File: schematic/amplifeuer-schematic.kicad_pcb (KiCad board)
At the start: 2 copper layers, 16 parts, among them J1 Input, J3 Output1, J4 Output2, J5 Power, U1 TDA1521A

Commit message: Move amplifier schematic 1 layer down
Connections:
- net +12V renamed /amplifier/+Vp
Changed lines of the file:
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@@
   (net 9 "Net-(C5-Pad2)")
   (net 10 GND)
-  (net 11 +12V)
-  (net 12 "Net-(C9-Pad1)")
-  (net 13 "Net-(C6-Pad2)")
+  (net 11 "Net-(C9-Pad1)")
+  (net 12 "Net-(C6-Pad2)")
+  (net 13 /amplifier/+Vp)
   (net_class Default "This is the default net class."
     (clearance 0.2)
@@
     (uvia_dia 0.3)
     (uvia_drill 0.1)
-    (add_net +12V)
+    (add_net /amplifier/+Vp)
     (add_net GND)
     (add_net "Net-(C1-Pad1)")
@@
       (net 10 GND))
     (pad 1 thru_hole rect (at 0 0) (size 1.7 1.7) (drill 1) (layers *.Cu *.Mask)
-      (net 13 "Net-(C6-Pad2)"))
+      (net 12 "Net-(C6-Pad2)"))
     (model ${KISYS3DMOD}/Connector_PinHeader_2.54mm.3dshapes/PinHeader_1x02_P2.54mm_Vertical.wrl
       (at (xyz 0 0 0))
@@
       (net 10 GND))
     (pad 2 thru_hole oval (at 0 2.54) (size 1.7 1.7) (drill 1) (layers *.Cu *.Mask)
-      (net 11 +12V))
+      (net 13 /amplifier/+Vp))
     (model ${KISYS3DMOD}/Connector_PinHeader_2.54mm.3dshapes/PinHeader_1x02_P2.54mm_Vertical.wrl
       (at (xyz 0 0 0))
@@
       (net 1 "Net-(C1-Pad2)"))
     (pad 2 thru_hole oval (at 0 2.54 90) (size 1.7 1.7) (drill 1) (layers *.Cu *.Mask)
-      (net 12 "Net-(C9-Pad1)"))
+      (net 11 "Net-(C9-Pad1)"))
     (pad 3 thru_hole oval (at 0 5.08 90) (size 1.7 1.7) (drill 1) (layers *.Cu *.Mask)
-      (net 12 "Net-(C9-Pad1)"))
+      (net 11 "Net-(C9-Pad1)"))
     (pad 4 thru_hole oval (at 0 7.62 90) (size 1.7 1.7) (drill 1) (layers *.Cu *.Mask)
       (net 5 "Net-(C3-Pad1)"))
@@
       (net 9 "Net-(C5-Pad2)"))
     (pad 7 thru_hole oval (at 0 15.24 90) (size 1.7 1.7) (drill 1) (layers *.Cu *.Mask)
-      (net 11 +12V))
+      (net 13 /amplifier/+Vp))
     (pad 8 thru_hole oval (at 0 17.78 90) (size 1.7 1.7) (drill 1) (layers *.Cu *.Mask)
-      (net 12 "Net-(C9-Pad1)"))
+      (net 11 "Net-(C9-Pad1)"))
     (pad 9 thru_hole oval (at 0 20.32 90) (size 1.7 1.7) (drill 1) (layers *.Cu *.Mask)
       (net 4 "Net-(C2-Pad2)"))
@@
       (net 9 "Net-(C5-Pad2)"))
     (pad 2 thru_hole circle (at 5 0 270) (size 2 2) (drill 1) (layers *.Cu *.Mask)
-      (net 13 "Net-(C6-Pad2)"))
+      (net 12 "Net-(C6-Pad2)"))
     (model ${KISYS3DMOD}/Capacitor_THT.3dshapes/CP_Radial_D10.0mm_P5.00mm.wrl
       (at (xyz 0 0 0))
@@
     )
     (pad 1 thru_hole rect (at 0 0 270) (size 2 2) (drill 1) (layers *.Cu *.Mask)
-      (net 11 +12V))
+      (net 13 /amplifier/+Vp))
     (pad 2 thru_hole circle (at 5 0 270) (size 2 2) (drill 1) (layers *.Cu *.Mask)
       (net 10 GND))
@@
     )
     (pad 1 thru_hole circle (at 0 0 180) (size 2 2) (drill 1) (layers *.Cu *.Mask)
-      (net 11 +12V))
+      (net 13 /amplifier/+Vp))
     (pad 2 thru_hole circle (at 5 0 180) (size 2 2) (drill 1) (layers *.Cu *.Mask)
       (net 10 GND))
@@
     )
     (pad 1 thru_hole rect (at 0 0) (size 1.6 1.6) (drill 0.8) (layers *.Cu *.Mask)
-      (net 12 "Net-(C9-Pad1)"))
+      (net 11 "Net-(C9-Pad1)"))
     (pad 2 thru_hole circle (at 2.5 0) (size 1.6 1.6) (drill 0.8) (layers *.Cu *.Mask)
       (net 10 GND))
@@
   (segment (start 184.15 94) (end 187.865001 90.284999) (width 0.25) (layer B.Cu) (net 10))
   (segment (start 184.15 95.25) (end 184.15 94) (width 0.25) (layer B.Cu) (net 10))
-  (segment (start 171.45 74.93) (end 171.45 77.47) (width 0.25) (layer F.Cu) (net 11))
-  (segment (start 181.61 77.47) (end 186.69 82.55) (width 0.25) (layer B.Cu) (net 11))
-  (segment (start 171.45 77.47) (end 181.61 77.47) (width 0.25) (layer B.Cu) (net 11))
-  (segment (start 184.15 85.09) (end 186.69 82.55) (width 0.25) (layer F.Cu) (net 11))
-  (segment (start 184.15 90.25) (end 184.15 85.09) (width 0.25) (layer F.Cu) (net 11))
-  (segment (start 161.29 74.93) (end 158.75 74.93) (width 0.25) (layer F.Cu) (net 12))
-  (segment (start 162.139999 74.080001) (end 161.29 74.93) (width 0.25) (layer B.Cu) (net 12))
-  (segment (start 163.83 72.39) (end 162.139999 74.080001) (width 0.25) (layer B.Cu) (net 12))
-  (segment (start 171.45 72.39) (end 163.83 72.39) (width 0.25) (layer B.Cu) (net 12))
-  (segment (start 173.99 74.93) (end 171.45 72.39) (width 0.25) (layer B.Cu) (net 12))
-  (segment (start 161.29 71.12) (end 161.29 74.93) (width 0.25) (layer F.Cu) (net 12))
-  (segment (start 161.29 71.12) (end 161.29 68.58) (width 0.25) (layer F.Cu) (net 12))
-  (segment (start 176.53 85.09) (end 176.53 92.71) (width 0.25) (layer F.Cu) (net 13))
+  (segment (start 171.45 74.93) (end 171.45 77.47) (width 0.25) (layer F.Cu) (net 13))
+  (segment (start 181.61 77.47) (end 186.69 82.55) (width 0.25) (layer B.Cu) (net 13))
+  (segment (start 171.45 77.47) (end 181.61 77.47) (width 0.25) (layer B.Cu) (net 13))
+  (segment (start 184.15 85.09) (end 186.69 82.55) (width 0.25) (layer F.Cu) (net 13))
+  (segment (start 184.15 90.25) (end 184.15 85.09) (width 0.25) (layer F.Cu) (net 13))
+  (segment (start 161.29 74.93) (end 158.75 74.93) (width 0.25) (layer F.Cu) (net 11))
+  (segment (start 162.139999 74.080001) (end 161.29 74.93) (width 0.25) (layer B.Cu) (net 11))
+  (segment (start 163.83 72.39) (end 162.139999 74.080001) (width 0.25) (layer B.Cu) (net 11))
+  (segment (start 171.45 72.39) (end 163.83 72.39) (width 0.25) (layer B.Cu) (net 11))
+  (segment (start 173.99 74.93) (end 171.45 72.39) (width 0.25) (layer B.Cu) (net 11))
+  (segment (start 161.29 71.12) (end 161.29 74.93) (width 0.25) (layer F.Cu) (net 11))
+  (segment (start 161.29 71.12) (end 161.29 68.58) (width 0.25) (layer F.Cu) (net 11))
+  (segment (start 176.53 85.09) (end 176.53 92.71) (width 0.25) (layer F.Cu) (net 12))
 )

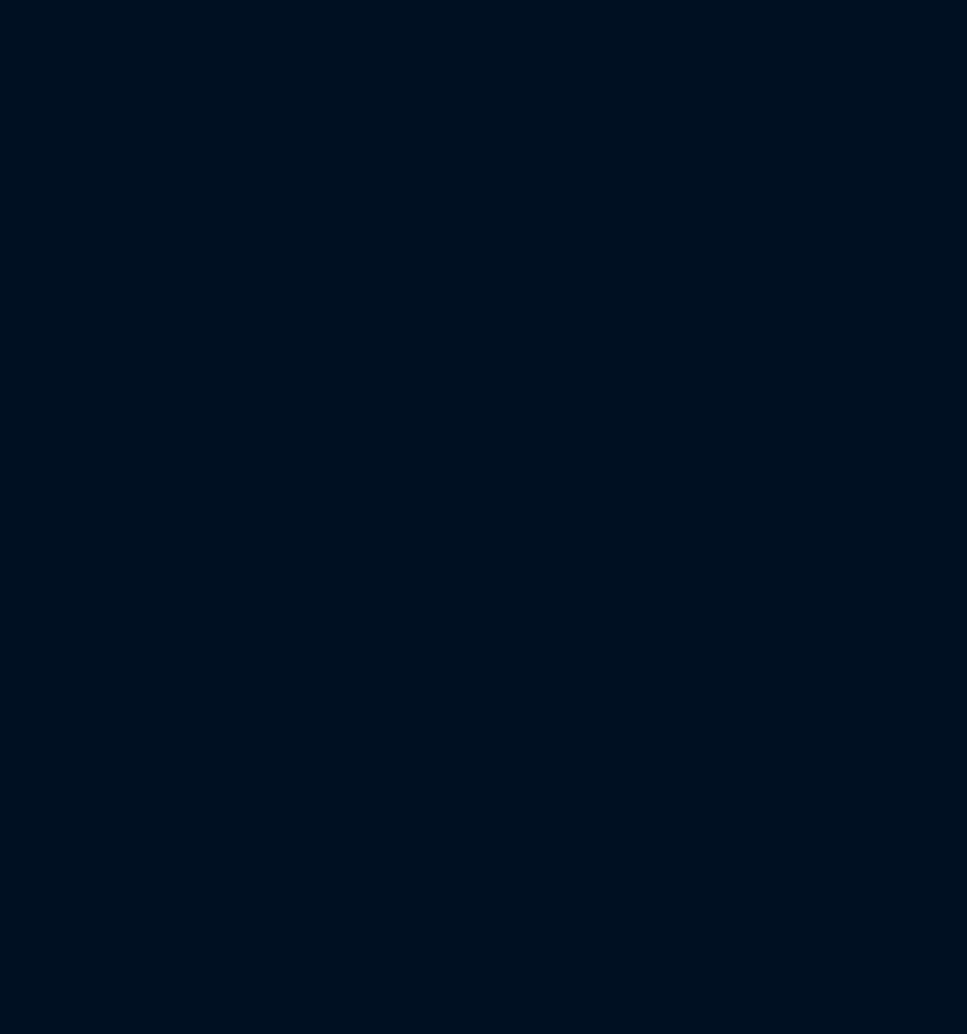
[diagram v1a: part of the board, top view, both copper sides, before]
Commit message: Add rudimentary PSU schematic and layout
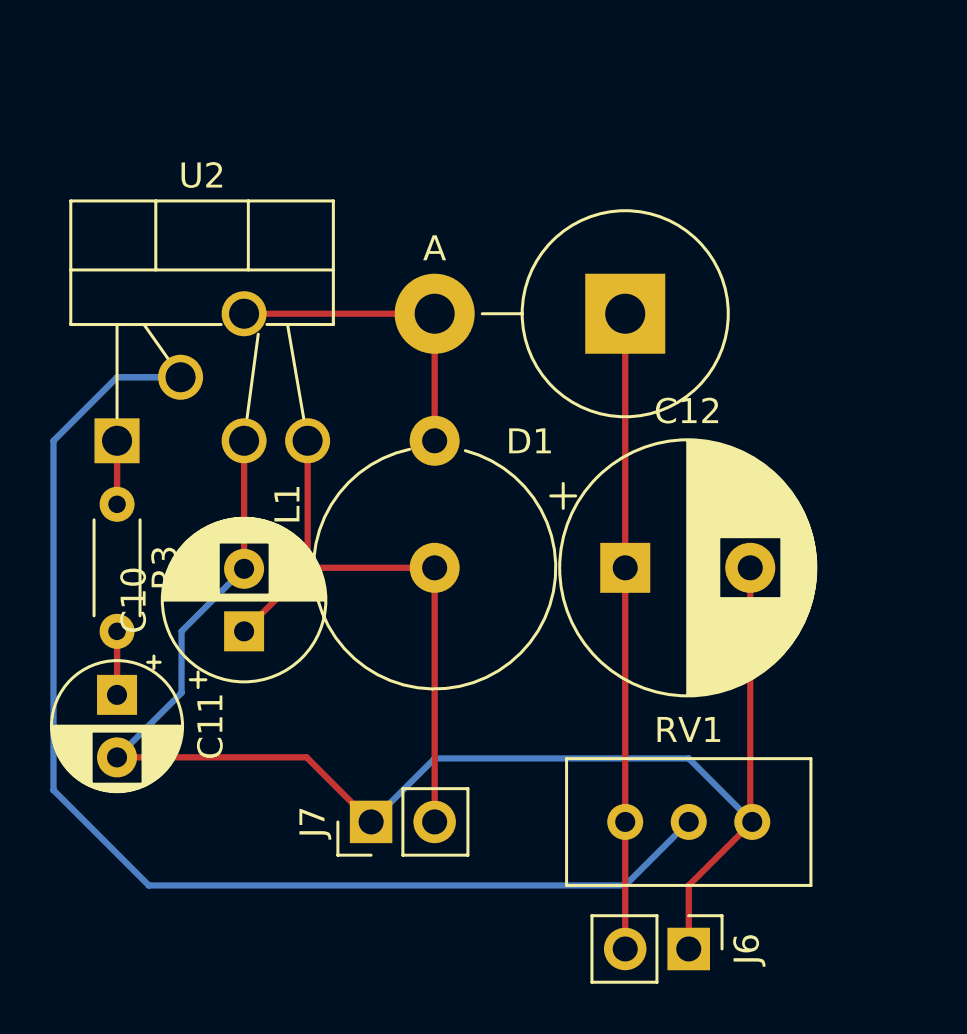
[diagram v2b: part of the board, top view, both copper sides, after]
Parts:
- added C10: 100μF, Capacitor_THT:CP_Radial_D6.3mm_P2.50mm, F.Cu at (105.4, 87.6)
- added C11: 1μF, Capacitor_THT:CP_Radial_D5.0mm_P2.50mm, F.Cu at (100.3, 90.2)
- added C12: 1000μF, Capacitor_THT:CP_Radial_D10.0mm_P5.00mm, F.Cu at (120.7, 85.1)
- added D1: D_Schottky, Diode_THT:D_5KPW_P7.62mm_Vertical_AnodeUp, F.Cu at (120.7, 74.9)
- added J6: Power out, Connector_PinHeader_2.54mm:PinHeader_1x02_P2.54mm_Vertical, F.Cu at (123.2, 100.3)
- added J7: Power in, Connector_PinHeader_2.54mm:PinHeader_1x02_P2.54mm_Vertical, F.Cu at (110.5, 95.2)
- added L1: L_Core_Ferrite, Inductor_THT:L_Axial_L16.0mm_D9.5mm_P5.08mm_Vertical_Vishay_IM-10-37, F.Cu at (113.0, 85.1)
- added R3: 1000R, Resistor_THT:R_Axial_DIN0204_L3.6mm_D1.6mm_P5.08mm_Horizontal, F.Cu at (100.3, 82.5)
- added RV1: R_POT_TRIM, Potentiometer_THT:Potentiometer_Bourns_3296W_Vertical, F.Cu at (125.7, 95.2)
- added U2: LT1071, Package_TO_SOT_THT:TO-220-5_PitchAligned, F.Cu at (100.3, 80.0)
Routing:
- net GND: track 94.5 -> 253.9 mm
- net /amplifier/+Vp: track 28.6 -> 167.4 mm
- net Net-(RV1-Pad2): track 0.00 -> 48.1 mm
- net +12V: track 0.00 -> 23.9 mm
- net Net-(D1-Pad2): track 0.00 -> 12.7 mm
- net Net-(C11-Pad1): track 0.00 -> 2.54 mm
- net Net-(R3-Pad1): track 0.00 -> 2.54 mm
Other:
- copper layers 2 -> 4

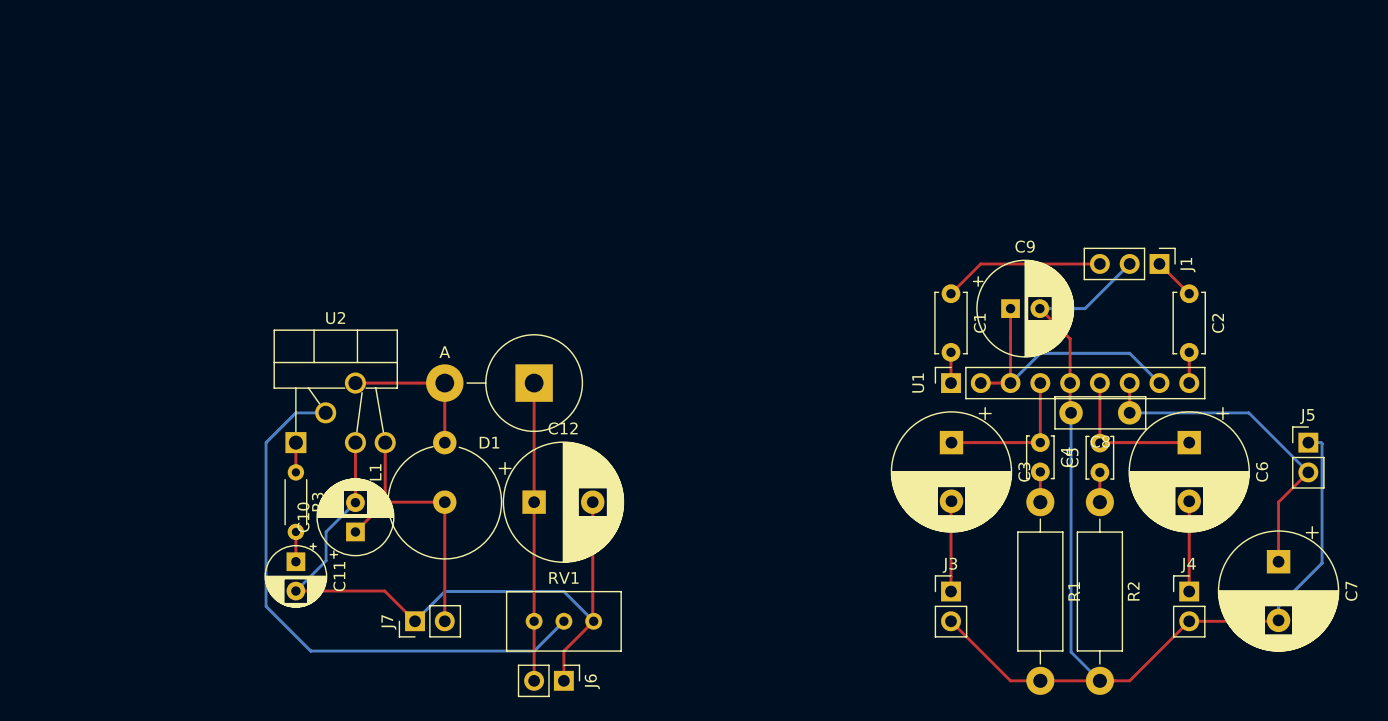
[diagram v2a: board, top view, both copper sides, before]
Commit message: Update all models on PCB to use WRL models
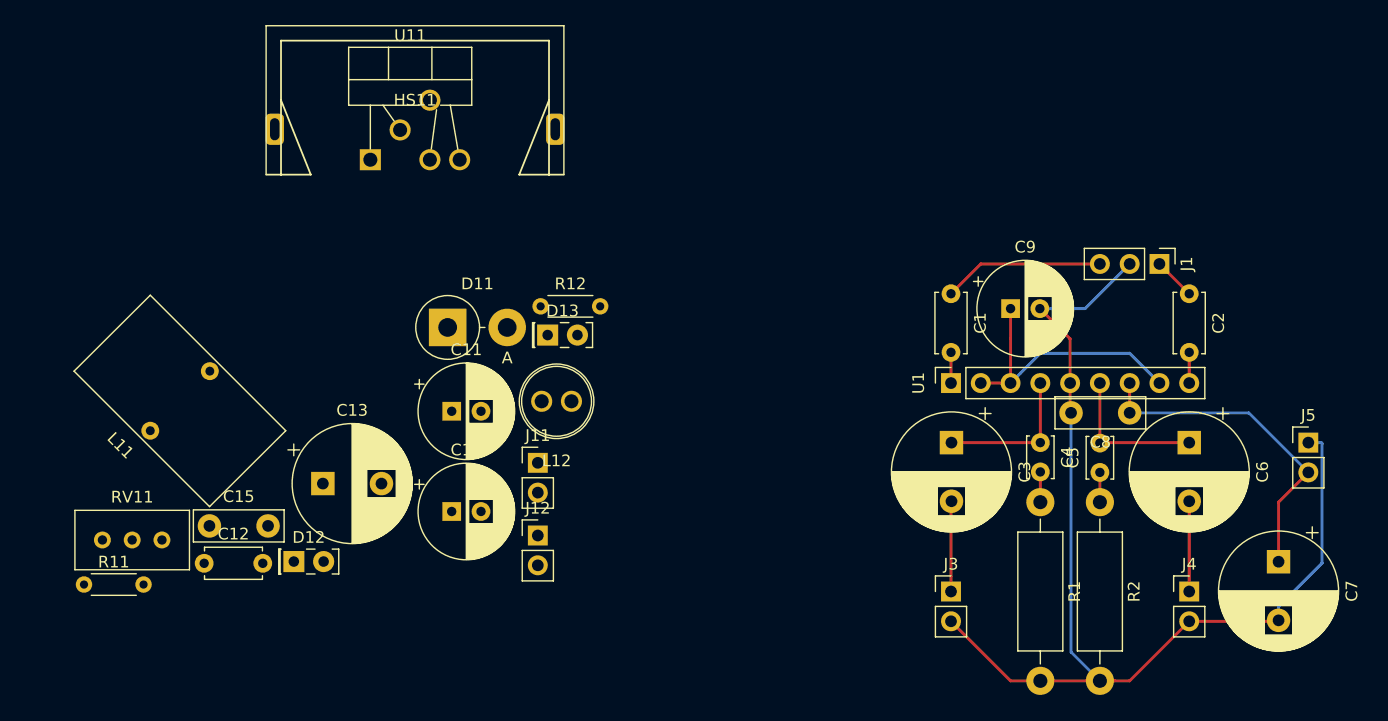
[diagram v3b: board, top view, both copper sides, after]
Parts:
- removed C10: 100μF, Capacitor_THT:CP_Radial_D6.3mm_P2.50mm
- removed D1: D_Schottky, Diode_THT:D_5KPW_P7.62mm_Vertical_AnodeUp
- removed J6: Power out, Connector_PinHeader_2.54mm:PinHeader_1x02_P2.54mm_Vertical
- removed J7: Power in, Connector_PinHeader_2.54mm:PinHeader_1x02_P2.54mm_Vertical
- removed L1: L_Core_Ferrite, Inductor_THT:L_Axial_L16.0mm_D9.5mm_P5.08mm_Vertical_Vishay_IM-10-37
- removed R3: 1000R, Resistor_THT:R_Axial_DIN0204_L3.6mm_D1.6mm_P5.08mm_Horizontal
- removed RV1: R_POT_TRIM, Potentiometer_THT:Potentiometer_Bourns_3296W_Vertical
- removed U2: LT1071, Package_TO_SOT_THT:TO-220-5_PitchAligned
- added C13: 1000μF, Capacitor_THT:CP_Radial_D10.0mm_P5.00mm, F.Cu at (102.6, 83.5)
- added C14: 100μF, Capacitor_THT:CP_Radial_D8.0mm_P2.50mm, F.Cu at (113.6, 85.9)
- added C15: 100nF, Capacitor_THT:C_Disc_D7.5mm_W2.5mm_P5.00mm, F.Cu at (93.0, 87.1)
- added D11: 1N5822, Diode_THT:D_DO-201AD_P5.08mm_Vertical_AnodeUp, F.Cu at (113.3, 70.2)
- added D12: Red, LED_THT:LED_Rectangular_W5.0mm_H2.0mm, F.Cu at (100.2, 90.2)
- added D13: Green, LED_THT:LED_Rectangular_W5.0mm_H2.0mm, F.Cu at (121.8, 70.8)
- added HS11: Aavid-5342B, Heatsink:Heatsink_Aavid-5342-TO220_Vertical, F.Cu at (110.5, 50.8)
- added J11: Power out, Connector_PinHeader_2.54mm:PinHeader_1x02_P2.54mm_Vertical, F.Cu at (121.0, 81.7)
- added J12: Power in, Connector_PinHeader_2.54mm:PinHeader_1x02_P2.54mm_Vertical, F.Cu at (121.0, 87.9)
- added L11: 100μH, Inductor_THT:L_Toroid_Vertical_L14.5mm_W7.0mm_P7.18mm, F.Cu at (90.4, 76.5)
- added L12: 10μH, Inductor_THT:L_Radial_D6.8mm_5.0mm_P2.54mm_sleeved, F.Cu at (122.6, 76.5)
- added R11: 1000R, Resistor_THT:R_Axial_DIN0204_L3.6mm_D1.6mm_P5.08mm_Horizontal, F.Cu at (82.3, 92.1)
- added R12: 2200R, Resistor_THT:R_Axial_DIN0204_L3.6mm_D1.6mm_P5.08mm_Horizontal, F.Cu at (121.2, 68.4)
- added RV11: 5000RTRIM, Potentiometer_THT:Potentiometer_Bourns_3296W_Vertical, F.Cu at (88.9, 88.3)
- added U11: LT1071, Package_TO_SOT_THT:TO-220-5_PitchAligned, F.Cu at (106.7, 55.9)
- C11: value 1μF -> 100μF; footprint Capacitor_THT:CP_Radial_D5.0mm_P2.50mm -> Capacitor_THT:CP_Radial_D8.0mm_P2.50mm
- C12: value 1000μF -> 1μF; footprint Capacitor_THT:CP_Radial_D10.0mm_P5.00mm -> Capacitor_THT:C_Disc_D4.7mm_W2.5mm_P5.00mm
- moved C12 28.6 mm to (92.5, 90.3)
- moved C11 18.5 mm to (113.6, 77.3), turned to 0 degrees
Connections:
- C11 pad 1: Net-(C11-Pad1) -> +12V
- C12 pad 1: /amplifier/+Vp -> Net-(C12-Pad1)
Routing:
- net GND: track 253.9 -> 183.5 mm
- net Net-(RV1-Pad2): track 48.1 -> 0.00 mm
- net /amplifier/+Vp: track 167.4 -> 129.4 mm
- net +12V: track 23.9 -> 0.00 mm
- net Net-(D1-Pad2): track 12.7 -> 0.00 mm
- net Net-(C11-Pad1): track 2.54 -> 0.00 mm
- net Net-(R3-Pad1): track 2.54 -> 0.00 mm

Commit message: Lay out PSU
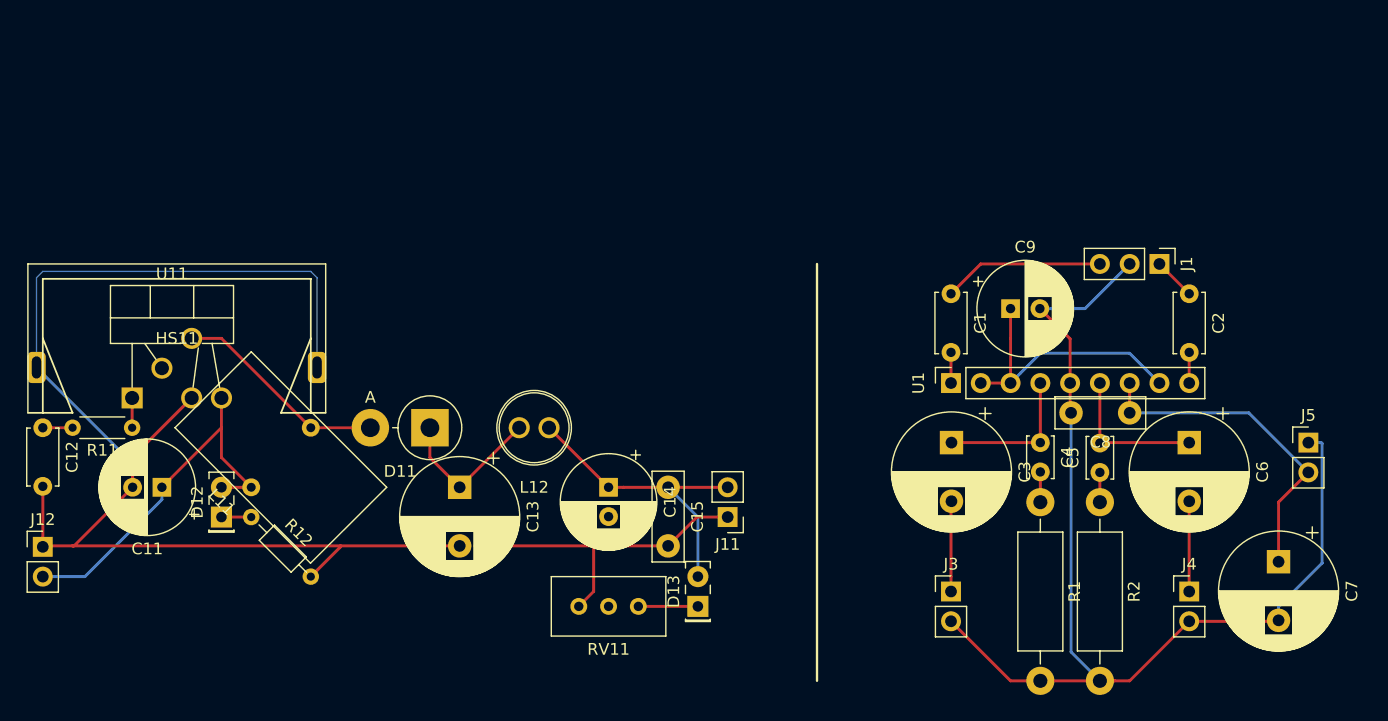
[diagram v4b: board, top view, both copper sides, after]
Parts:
- R12: footprint Resistor_THT:R_Axial_DIN0204_L3.6mm_D1.6mm_P5.08mm_Horizontal -> Resistor_THT:R_Axial_DIN0204_L3.6mm_D1.6mm_P7.62mm_Horizontal
- moved J12 42.2 mm to (78.7, 88.9)
- moved C15 39.3 mm to (132.1, 83.8), turned to 270 degrees
- moved RV11 36.0 mm to (124.5, 94.0), turned to 180 degrees
- moved R12 30.5 mm to (96.5, 86.4), turned to 315 degrees
- moved U11 28.7 mm to (86.4, 76.2)
- moved HS11 28.7 mm to (90.2, 71.1)
- moved D13 26.5 mm to (134.6, 94.0), turned to 90 degrees
- moved C11 25.6 mm to (88.9, 83.8), turned to 180 degrees
- moved C12 18.0 mm to (78.7, 78.7), turned to 270 degrees
- moved J11 16.8 mm to (137.2, 86.4), turned to 180 degrees
- moved R11 14.0 mm to (86.4, 78.7), turned to 180 degrees
- moved C14 13.5 mm to (127.0, 83.8), turned to 270 degrees
- moved C13 11.7 mm to (114.3, 83.8), turned to 270 degrees
- moved L11 9.87 mm to (99.1, 81.3)
- moved D11 8.69 mm to (111.8, 78.7), turned to 180 degrees
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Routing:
- net GND: track 183.5 -> 293.8 mm
- net Net-(RV11-Pad2): track 0.00 -> 63.6 mm
- net +12V: track 0.00 -> 32.3 mm
- net Net-(D11-Pad2): track 0.00 -> 18.4 mm
- net /amplifier/+Vp: track 129.4 -> 113.9 mm
- net Net-(C13-Pad1): track 0.00 -> 13.3 mm
- net Net-(D13-Pad1): track 0.00 -> 5.08 mm
- net Net-(C12-Pad1): track 0.00 -> 2.54 mm
- net Net-(R11-Pad1): track 0.00 -> 2.54 mm
- net Net-(D12-Pad1): track 0.00 -> 2.54 mm
